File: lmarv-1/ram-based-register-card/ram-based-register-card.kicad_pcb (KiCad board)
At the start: 4 copper layers, 125.4 x 41.3 mm, 18 parts, among them P1 dual-pcie-cardedge, U1 IDT70V24_TQ100, U2 IDT70V24_TQ100, U3 IDT70V24_TQ100, U4 IDT70V24_TQ100

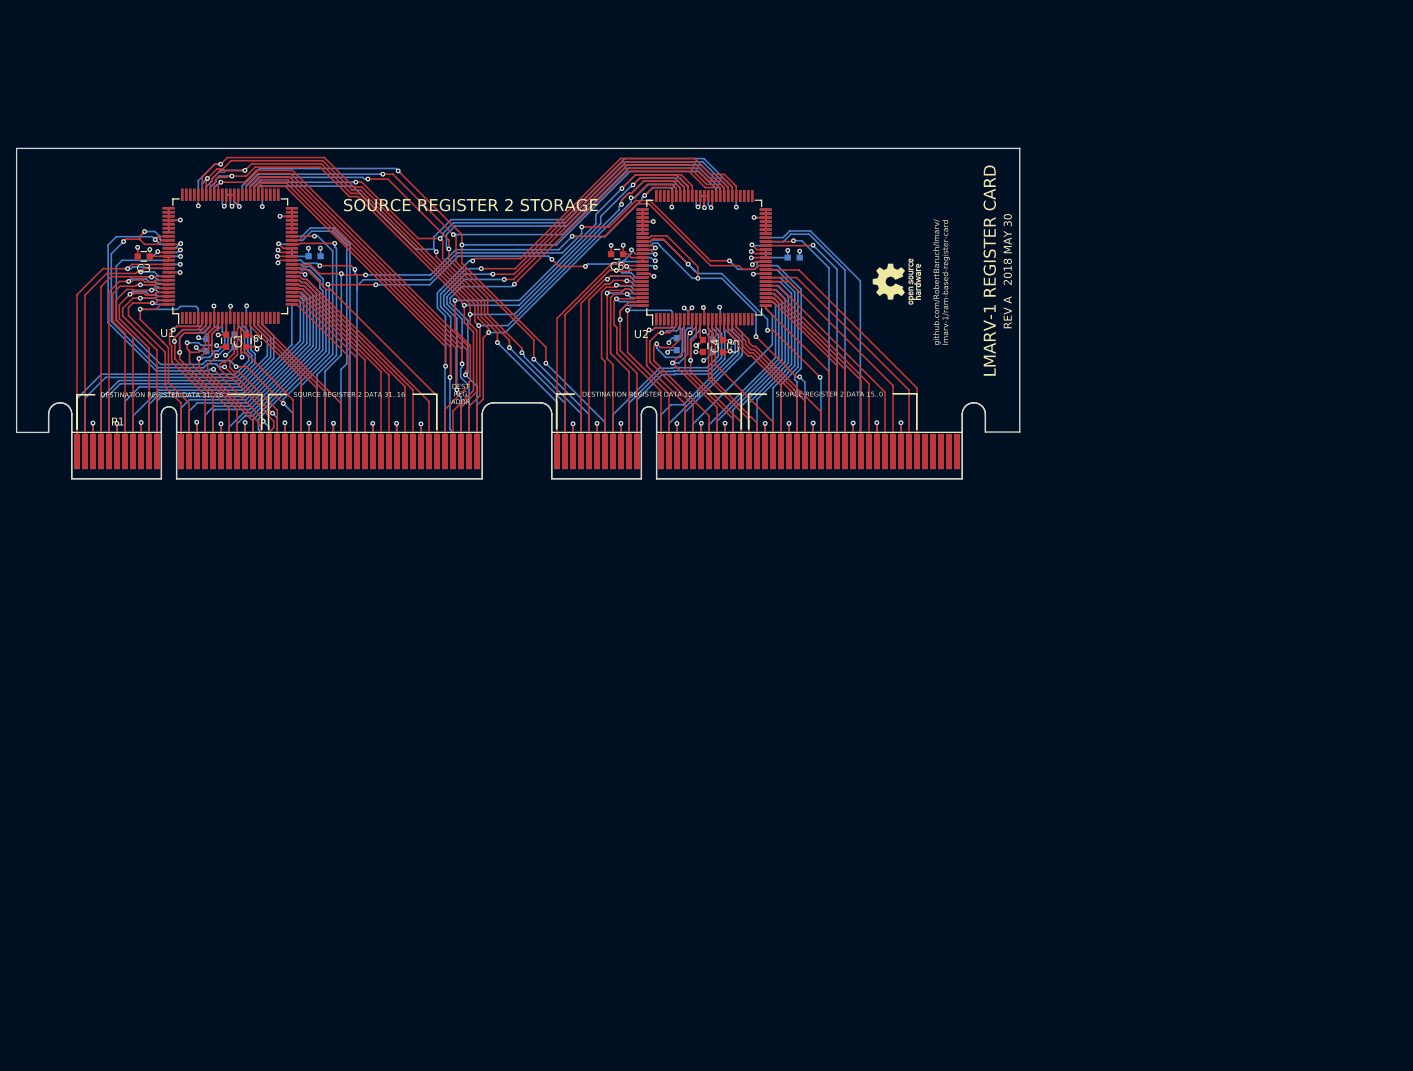
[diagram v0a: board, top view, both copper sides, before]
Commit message: ALU rev D, with simulations
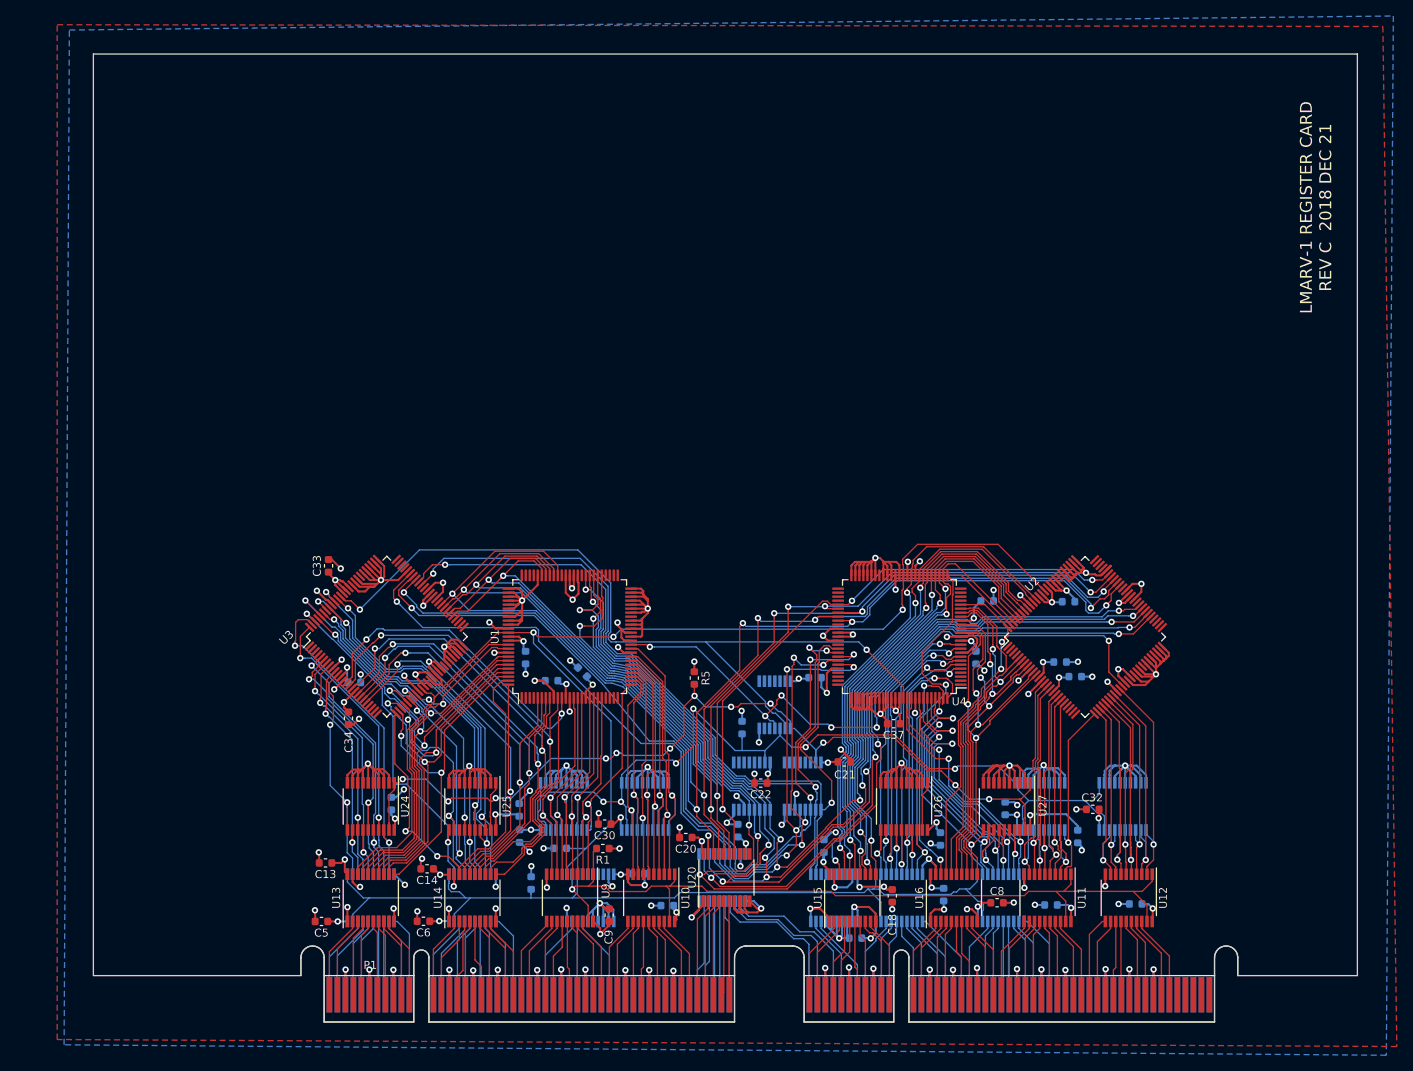
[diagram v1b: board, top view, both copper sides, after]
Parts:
- removed REF***: OSHW-Logo_5.7x6mm_SilkScreen, Symbols:OSHW-Logo_5.7x6mm_SilkScreen
- added C13: 0u1, Capacitor_SMD:C_0603_1608Metric, F.Cu at (93.0, 131.1)
- added C14: 0u1, Capacitor_SMD:C_0603_1608Metric, F.Cu at (105.7, 131.9)
- added C15: 0u1, Capacitor_SMD:C_0603_1608Metric, B.Cu at (155.3, 129.0)
- added C16: 0u1, Capacitor_SMD:C_0603_1608Metric, B.Cu at (170.3, 135.1)
- added C17: 0u1, Capacitor_SMD:C_0603_1608Metric, B.Cu at (132.1, 132.5)
- added C18: 0u1, Capacitor_SMD:C_0603_1608Metric, F.Cu at (163.9, 135.2)
- added C19: 0u1, Capacitor_SMD:C_0603_1608Metric, B.Cu at (144.6, 127.1)
- added C20: 0u1, Capacitor_SMD:C_0603_1608Metric, F.Cu at (138.0, 127.9)
- added C21: 0u1, Capacitor_SMD:C_0603_1608Metric, F.Cu at (157.9, 118.5)
- added C22: 0u1, Capacitor_SMD:C_0603_1608Metric, F.Cu at (147.4, 121.1)
- added C23: 0u1, Capacitor_SMD:C_0603_1608Metric, B.Cu at (154.2, 108.0)
- added C24: 0u1, Capacitor_SMD:C_0603_1608Metric, B.Cu at (101.2, 123.7)
- added C25: 0u1, Capacitor_SMD:C_0603_1608Metric, B.Cu at (117.2, 124.5)
- added C26: 0u1, Capacitor_SMD:C_0603_1608Metric, B.Cu at (169.9, 128.1)
- added C27: 0u1, Capacitor_SMD:C_0603_1608Metric, B.Cu at (187.0, 127.8)
- added C28: 0u1, Capacitor_SMD:C_0603_1608Metric, B.Cu at (186.7, 107.8)
- added C29: 0u1, Capacitor_SMD:C_0603_1608Metric, B.Cu at (117.3, 127.8)
- added C30: 0u1, Capacitor_SMD:C_0603_1608Metric, F.Cu at (127.9, 126.3)
- added C31: 0u1, Capacitor_SMD:C_0603_1608Metric, B.Cu at (178.0, 124.3)
- added C32: 0u1, Capacitor_SMD:C_0603_1608Metric, F.Cu at (188.9, 124.4)
- added C33: 0u1, Capacitor_SMD:C_0603_1608Metric, F.Cu at (93.4, 94.0)
- added C34: 0u1, Capacitor_SMD:C_0603_1608Metric, F.Cu at (95.9, 113.0)
- added C35: 0u1, Capacitor_SMD:C_0603_1608Metric, B.Cu at (185.9, 98.5)
- added C36: 0u1, Capacitor_SMD:C_0603_1608Metric, B.Cu at (184.8, 106.0)
- added C37: 0u1, Capacitor_SMD:C_0603_1608Metric, F.Cu at (164.0, 113.7)
- added C38: 0u1, Capacitor_SMD:C_0603_1608Metric, B.Cu at (175.7, 98.4)
- added C39: 0u1, Capacitor_SMD:C_0603_1608Metric, B.Cu at (174.3, 105.4)
- added R1: 47k, Resistor_SMD:R_0603_1608Metric, F.Cu at (127.7, 129.3)
- added R2: 47k, Resistor_SMD:R_0603_1608Metric, B.Cu at (118.7, 133.6)
- added R3: 47k, Resistor_SMD:R_0603_1608Metric, B.Cu at (122.4, 129.3)
- added R4: 47k, Resistor_SMD:R_0603_1608Metric, B.Cu at (145.1, 114.2)
- added R5: 47k, Resistor_SMD:R_0603_1608Metric, F.Cu at (139.1, 108.0)
- added U10: 74LVC541_a, Package_SO:TSSOP-20_4.4x6.5mm_P0.65mm, F.Cu at (133.7, 135.5)
- added U11: 74LVC541_a, Package_SO:TSSOP-20_4.4x6.5mm_P0.65mm, F.Cu at (183.3, 135.5)
- added U12: 74LVC541_a, Package_SO:TSSOP-20_4.4x6.5mm_P0.65mm, F.Cu at (193.4, 135.5)
- added U13: 74LVC541, Package_SO:TSSOP-20_4.4x6.5mm_P0.65mm, F.Cu at (98.7, 135.5)
- added U14: 74LVC541, Package_SO:TSSOP-20_4.4x6.5mm_P0.65mm, F.Cu at (111.4, 135.5)
- added U15: 74LVC541, Package_SO:TSSOP-20_4.4x6.5mm_P0.65mm, F.Cu at (158.9, 135.5)
- added U16: 74LVC541, Package_SO:TSSOP-20_4.4x6.5mm_P0.65mm, F.Cu at (171.6, 135.5)
- added U17: 74LVC541, Package_SO:TSSOP-20_4.4x6.5mm_P0.65mm, B.Cu at (126.1, 135.5)
- added U18: 74LVC541, Package_SO:TSSOP-20_4.4x6.5mm_P0.65mm, B.Cu at (156.6, 135.5)
- added U19: 74LVC541, Package_SO:TSSOP-20_4.4x6.5mm_P0.65mm, B.Cu at (142.6, 132.9)
- added U20: 74LVC541, Package_SO:TSSOP-20_4.4x6.5mm_P0.65mm, F.Cu at (143.1, 132.9)
- added U21: 74LVC138, Package_SO:TSSOP-16_4.4x5mm_P0.65mm, B.Cu at (152.7, 121.5)
- added U22: 74LVC138, Package_SO:TSSOP-16_4.4x5mm_P0.65mm, B.Cu at (146.3, 121.5)
- added U23: 74LVC04, Package_SO:TSSOP-14_4.4x5mm_P0.65mm, B.Cu at (149.2, 111.3)
- added U24: 74LVC541_a, Package_SO:TSSOP-20_4.4x6.5mm_P0.65mm, F.Cu at (98.7, 124.0)
- added U25: 74LVC541_a, Package_SO:TSSOP-20_4.4x6.5mm_P0.65mm, F.Cu at (111.4, 124.0)
- added U26: 74LVC541_a, Package_SO:TSSOP-20_4.4x6.5mm_P0.65mm, F.Cu at (165.3, 124.0)
- added U27: 74LVC541_a, Package_SO:TSSOP-20_4.4x6.5mm_P0.65mm, F.Cu at (178.2, 124.0)
- added U29: 74LVC541, Package_SO:TSSOP-20_4.4x6.5mm_P0.65mm, B.Cu at (122.8, 124.0)
- added U30: 74LVC541, Package_SO:TSSOP-20_4.4x6.5mm_P0.65mm, B.Cu at (133.0, 124.0)
- added U31: 74LVC541, Package_SO:TSSOP-20_4.4x6.5mm_P0.65mm, B.Cu at (182.5, 124.0)
- added U32: 74LVC541, Package_SO:TSSOP-20_4.4x6.5mm_P0.65mm, B.Cu at (192.7, 124.0)
- added U5: 74LVC541, Package_SO:TSSOP-20_4.4x6.5mm_P0.65mm, B.Cu at (98.7, 135.5)
- added U6: 74LVC541, Package_SO:TSSOP-20_4.4x6.5mm_P0.65mm, B.Cu at (111.4, 135.5)
- added U7: 74LVC541, Package_SO:TSSOP-20_4.4x6.5mm_P0.65mm, B.Cu at (164.7, 135.5)
- added U8: 74LVC541, Package_SO:TSSOP-20_4.4x6.5mm_P0.65mm, B.Cu at (177.4, 135.5)
- added U9: 74LVC541_a, Package_SO:TSSOP-20_4.4x6.5mm_P0.65mm, F.Cu at (123.6, 135.5)
- C1, C2, C3, C4: footprint Capacitors_SMD:C_0603 -> Capacitor_SMD:C_0603_1608Metric; moved to B.Cu
- C10, C11, C12, C5, C6, C7: footprint Capacitors_SMD:C_0603 -> Capacitor_SMD:C_0603_1608Metric
- C8, C9: footprint Capacitors_SMD:C_0603 -> Capacitor_SMD:C_0603_1608Metric; moved to F.Cu
- P1: value dual-pcie-cardedge -> dual-pcie-cardedge_split
- U1, U2: footprint Housings_QFP:TQFP-100_14x14mm_Pitch0.5mm -> Package_QFP:TQFP-100_14x14mm_P0.5mm
- U3, U4: footprint Housings_QFP:TQFP-100_14x14mm_Pitch0.5mm -> Package_QFP:TQFP-100_14x14mm_P0.5mm; moved to F.Cu
- moved C8 121.0 mm to (177.0, 136.1), turned to 0 degrees
- moved C7 107.7 mm to (159.3, 140.5), turned to 180 degrees
- moved C12 91.4 mm to (194.3, 136.2), turned to 180 degrees
- moved C9 90.2 mm to (128.5, 137.6), turned to 90 degrees
- moved C5 87.7 mm to (92.5, 138.4), turned to 180 degrees
- moved C6 86.8 mm to (105.3, 138.4)
- moved C11 81.7 mm to (183.7, 136.4), turned to 180 degrees
- moved C3 75.5 mm to (125.1, 107.3), turned to 135 degrees
- moved P1 74.9 mm to (105.0, 151.0)
- moved C10 70.2 mm to (135.7, 136.4), turned to 180 degrees
- moved U2 67.2 mm to (188.0, 102.9), turned to 45 degrees
- moved U1 63.7 mm to (123.5, 102.8)
- moved C4 60.6 mm to (96.6, 108.6), turned to 0 degrees
- moved C2 57.1 mm to (121.3, 108.3), turned to 180 degrees
- moved C1 54.5 mm to (118.0, 105.4)
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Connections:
- P1 pad 121: /~rd_bhh -> Net-(P1-Pad121)
- P1 pad 122: /~rd_bhl -> Net-(P1-Pad122)
- P1 pad 125: /~rs2_bhh -> Net-(P1-Pad125)
- P1 pad 127: /~rs2_bhl -> Net-(P1-Pad127)
- P1 pad 130: /~rs1_bhh -> Net-(P1-Pad130)
- P1 pad 131: /~rs1_bhl -> Net-(P1-Pad131)
- P1 pad 177: /~rd_blh -> Net-(P1-Pad177)
- P1 pad 179: /~rd_bll -> Net-(P1-Pad179)
- P1 pad 180: /~rs2_blh -> Net-(P1-Pad180)
- P1 pad 181: /~rs2_bll -> Net-(P1-Pad181)
- P1 pad 182: /~rs1_blh -> Net-(P1-Pad182)
- P1 pad 184: /~rs1_bll -> Net-(P1-Pad184)
- U1 pad 10: /rd[17] -> /rd[17]'
- U1 pad 100: /rd[22] -> /rd[22]'
- U1 pad 11: /rd[16] -> /rd[16]'
- U1 pad 14: /rs2[31] -> /rs2[31]'
- U1 pad 15: /rs2[30] -> /rs2[30]'
- U1 pad 16: /rs2[29] -> /rs2[29]'
- U1 pad 18: /rs2[28] -> /rs2[28]'
- U1 pad 19: /rs2[27] -> /rs2[27]'
- U1 pad 20: /rs2[26] -> /rs2[26]'
- U1 pad 21: /rs2[25] -> /rs2[25]'
- U1 pad 26: /rs2[24] -> /rs2[24]'
- U1 pad 27: /rs2[23] -> /rs2[23]'
- U1 pad 28: /rs2[22] -> /rs2[22]'
- U1 pad 29: /rs2[21] -> /rs2[21]'
- U1 pad 30: /rs2[20] -> /rs2[20]'
- U1 pad 31: /rs2[19] -> /rs2[19]'
- U1 pad 32: /rs2[18] -> /rs2[18]'
- U1 pad 33: /rs2[17] -> /rs2[17]'
- U1 pad 35: /rs2[16] -> /rs2[16]'
- U1 pad 36: /~rs2_rd -> /rs2_zero
- U1 pad 41: /~rs2_bhl -> GND
- U1 pad 42: /~rs2_bhh -> GND
- U1 pad 5: /rd[21] -> /rd[21]'
- U1 pad 55: /rs2a[4] -> /rs2a[4]'
- U1 pad 56: /rs2a[3] -> /rs2a[3]'
- U1 pad 57: /rs2a[2] -> /rs2a[2]'
- U1 pad 58: /rs2a[1] -> /rs2a[1]'
- U1 pad 59: /rs2a[0] -> /rs2a[0]'
- U1 pad 6: /rd[20] -> /rd[20]'
- U1 pad 66: /rda[0] -> /rda[0]'
- U1 pad 67: /rda[1] -> /rda[1]'
- U1 pad 68: /rda[2] -> /rda[2]'
- U1 pad 69: /rda[3] -> /rda[3]'
- U1 pad 7: /rd[19] -> /rd[19]'
- U1 pad 70: /rda[4] -> /rda[4]'
- U1 pad 8: /rd[18] -> /rd[18]'
- U1 pad 83: /~rd_bhh -> GND
- U1 pad 84: /~rd_bhl -> GND
- U1 pad 87: /~rd_wr -> /~rd_wr~'
- U1 pad 90: /rd[31] -> /rd[31]'
- U1 pad 91: /rd[30] -> /rd[30]'
- U1 pad 93: /rd[29] -> /rd[29]'
- U1 pad 94: /rd[28] -> /rd[28]'
- U1 pad 95: /rd[27] -> /rd[27]'
- U1 pad 96: /rd[26] -> /rd[26]'
- U1 pad 97: /rd[25] -> /rd[25]'
- U1 pad 98: /rd[24] -> /rd[24]'
- U1 pad 99: /rd[23] -> /rd[23]'
- U2 pad 10: /rd[1] -> /rd[1]'
- U2 pad 100: /rd[6] -> /rd[6]'
- U2 pad 11: /rd[0] -> /rd[0]'
- U2 pad 14: /rs2[15] -> /rs2[15]'
- U2 pad 15: /rs2[14] -> /rs2[14]'
- U2 pad 16: /rs2[13] -> /rs2[13]'
- U2 pad 18: /rs2[12] -> /rs2[12]'
- U2 pad 19: /rs2[11] -> /rs2[11]'
- U2 pad 20: /rs2[10] -> /rs2[10]'
- U2 pad 21: /rs2[9] -> /rs2[9]'
- U2 pad 26: /rs2[8] -> /rs2[8]'
- U2 pad 27: /rs2[7] -> /rs2[7]'
- U2 pad 28: /rs2[6] -> /rs2[6]'
- U2 pad 29: /rs2[5] -> /rs2[5]'
- U2 pad 30: /rs2[4] -> /rs2[4]'
- U2 pad 31: /rs2[3] -> /rs2[3]'
- U2 pad 32: /rs2[2] -> /rs2[2]'
- U2 pad 33: /rs2[1] -> /rs2[1]'
- U2 pad 35: /rs2[0] -> /rs2[0]'
- U2 pad 36: /~rs2_rd -> /rs2_zero
- U2 pad 41: /~rs2_bll -> GND
- U2 pad 42: /~rs2_blh -> GND
- U2 pad 5: /rd[5] -> /rd[5]'
- U2 pad 55: /rs2a[4] -> /rs2a[4]'
- U2 pad 56: /rs2a[3] -> /rs2a[3]'
- U2 pad 57: /rs2a[2] -> /rs2a[2]'
- U2 pad 58: /rs2a[1] -> /rs2a[1]'
- U2 pad 59: /rs2a[0] -> /rs2a[0]'
- U2 pad 6: /rd[4] -> /rd[4]'
- U2 pad 66: /rda[0] -> /rda[0]'
- U2 pad 67: /rda[1] -> /rda[1]'
- U2 pad 68: /rda[2] -> /rda[2]'
- U2 pad 69: /rda[3] -> /rda[3]'
- U2 pad 7: /rd[3] -> /rd[3]'
- U2 pad 70: /rda[4] -> /rda[4]'
- U2 pad 8: /rd[2] -> /rd[2]'
- U2 pad 83: /~rd_blh -> GND
- U2 pad 84: /~rd_bll -> GND
- U2 pad 87: /~rd_wr -> /~rd_wr~'
- U2 pad 90: /rd[15] -> /rd[15]'
- U2 pad 91: /rd[14] -> /rd[14]'
- U2 pad 93: /rd[13] -> /rd[13]'
- U2 pad 94: /rd[12] -> /rd[12]'
- U2 pad 95: /rd[11] -> /rd[11]'
- U2 pad 96: /rd[10] -> /rd[10]'
- U2 pad 97: /rd[9] -> /rd[9]'
- U2 pad 98: /rd[8] -> /rd[8]'
- U2 pad 99: /rd[7] -> /rd[7]'
- U3 pad 10: /rs1[30] -> /rs1[30]'
- U3 pad 100: /rs1[25] -> /rs1[25]'
- U3 pad 11: /rs1[31] -> /rs1[31]'
- U3 pad 14: /rd[16] -> /rd[16]'
- U3 pad 15: /rd[17] -> /rd[17]'
- U3 pad 16: /rd[18] -> /rd[18]'
- U3 pad 18: /rd[19] -> /rd[19]'
- U3 pad 19: /rd[20] -> /rd[20]'
- U3 pad 20: /rd[21] -> /rd[21]'
- U3 pad 21: /rd[22] -> /rd[22]'
- U3 pad 26: /rd[23] -> /rd[23]'
- U3 pad 27: /rd[24] -> /rd[24]'
- U3 pad 28: /rd[25] -> /rd[25]'
- U3 pad 29: /rd[26] -> /rd[26]'
- U3 pad 30: /rd[27] -> /rd[27]'
- U3 pad 31: /rd[28] -> /rd[28]'
- U3 pad 32: /rd[29] -> /rd[29]'
- U3 pad 33: /rd[30] -> /rd[30]'
- U3 pad 35: /rd[31] -> /rd[31]'
- U3 pad 37: /~rd_wr -> /~rd_wr~'
- U3 pad 41: /~rd_bhh -> GND
- U3 pad 42: /~rd_bhl -> GND
- U3 pad 5: /rs1[26] -> /rs1[26]'
- U3 pad 55: /rda[4] -> /rda[4]'
- U3 pad 56: /rda[3] -> /rda[3]'
- U3 pad 57: /rda[2] -> /rda[2]'
- U3 pad 58: /rda[1] -> /rda[1]'
- U3 pad 59: /rda[0] -> /rda[0]'
- U3 pad 6: /rs1[27] -> /rs1[27]'
- U3 pad 66: /rs1a[0] -> /rs1a[0]'
- U3 pad 67: /rs1a[1] -> /rs1a[1]'
- U3 pad 68: /rs1a[2] -> /rs1a[2]'
- U3 pad 69: /rs1a[3] -> /rs1a[3]'
- U3 pad 7: /rs1[28] -> /rs1[28]'
- U3 pad 70: /rs1a[4] -> /rs1a[4]'
- U3 pad 8: /rs1[29] -> /rs1[29]'
- U3 pad 83: /~rs1_bhl -> GND
- U3 pad 84: /~rs1_bhh -> GND
- U3 pad 89: /~rs1_rd -> /rs1_zero
- U3 pad 90: /rs1[16] -> /rs1[16]'
- U3 pad 91: /rs1[17] -> /rs1[17]'
- U3 pad 93: /rs1[18] -> /rs1[18]'
- U3 pad 94: /rs1[19] -> /rs1[19]'
- U3 pad 95: /rs1[20] -> /rs1[20]'
- U3 pad 96: /rs1[21] -> /rs1[21]'
- U3 pad 97: /rs1[22] -> /rs1[22]'
- U3 pad 98: /rs1[23] -> /rs1[23]'
- U3 pad 99: /rs1[24] -> /rs1[24]'
- U4 pad 10: /rs1[14] -> /rs1[14]'
- U4 pad 100: /rs1[9] -> /rs1[9]'
- U4 pad 11: /rs1[15] -> /rs1[15]'
- U4 pad 14: /rd[0] -> /rd[0]'
- U4 pad 15: /rd[1] -> /rd[1]'
- U4 pad 16: /rd[2] -> /rd[2]'
- U4 pad 18: /rd[3] -> /rd[3]'
- U4 pad 19: /rd[4] -> /rd[4]'
- U4 pad 20: /rd[5] -> /rd[5]'
- U4 pad 21: /rd[6] -> /rd[6]'
- U4 pad 26: /rd[7] -> /rd[7]'
- U4 pad 27: /rd[8] -> /rd[8]'
- U4 pad 28: /rd[9] -> /rd[9]'
- U4 pad 29: /rd[10] -> /rd[10]'
- U4 pad 30: /rd[11] -> /rd[11]'
- U4 pad 31: /rd[12] -> /rd[12]'
- U4 pad 32: /rd[13] -> /rd[13]'
- U4 pad 33: /rd[14] -> /rd[14]'
- U4 pad 35: /rd[15] -> /rd[15]'
- U4 pad 37: /~rd_wr -> /~rd_wr~'
- U4 pad 41: /~rd_blh -> GND
- U4 pad 42: /~rd_bll -> GND
- U4 pad 5: /rs1[10] -> /rs1[10]'
- U4 pad 55: /rda[4] -> /rda[4]'
- U4 pad 56: /rda[3] -> /rda[3]'
- U4 pad 57: /rda[2] -> /rda[2]'
- U4 pad 58: /rda[1] -> /rda[1]'
- U4 pad 59: /rda[0] -> /rda[0]'
- U4 pad 6: /rs1[11] -> /rs1[11]'
- U4 pad 66: /rs1a[0] -> /rs1a[0]'
- U4 pad 67: /rs1a[1] -> /rs1a[1]'
- U4 pad 68: /rs1a[2] -> /rs1a[2]'
- U4 pad 69: /rs1a[3] -> /rs1a[3]'
- U4 pad 7: /rs1[12] -> /rs1[12]'
- U4 pad 70: /rs1a[4] -> /rs1a[4]'
- U4 pad 8: /rs1[13] -> /rs1[13]'
- U4 pad 83: /~rs1_bll -> GND
- U4 pad 84: /~rs1_blh -> GND
- U4 pad 89: /~rs1_rd -> /rs1_zero
- U4 pad 90: /rs1[0] -> /rs1[0]'
- U4 pad 91: /rs1[1] -> /rs1[1]'
- U4 pad 93: /rs1[2] -> /rs1[2]'
- U4 pad 94: /rs1[3] -> /rs1[3]'
- U4 pad 95: /rs1[4] -> /rs1[4]'
- U4 pad 96: /rs1[5] -> /rs1[5]'
- U4 pad 97: /rs1[6] -> /rs1[6]'
- U4 pad 98: /rs1[7] -> /rs1[7]'
- U4 pad 99: /rs1[8] -> /rs1[8]'
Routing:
- net GND: track 222.0 -> 706.3 mm, vias 56 -> 113
- net /rda[0]': track 0.00 -> 153.0 mm, vias 0 -> 5
- net /rda[1]': track 0.00 -> 148.5 mm, vias 0 -> 5
- net /rda[2]': track 0.00 -> 145.4 mm, vias 0 -> 5
- net /rs2a[4]': track 0.00 -> 139.5 mm, vias 0 -> 5
- net /rda[3]': track 0.00 -> 138.9 mm, vias 0 -> 5
- net /rs2a[2]': track 0.00 -> 136.2 mm, vias 0 -> 5
- net /rs2a[3]': track 0.00 -> 134.9 mm, vias 0 -> 5
- net /rda[4]': track 0.00 -> 133.5 mm, vias 0 -> 4
- net /~rd_wr~': track 0.00 -> 130.4 mm, vias 0 -> 3
- net /rs2a[1]': track 0.00 -> 128.8 mm, vias 0 -> 5
- net /rs2a[0]': track 0.00 -> 126.8 mm, vias 0 -> 5
- net /~rs1_zero: track 0.00 -> 126.6 mm, vias 0 -> 12
- net /~rs2_zero: track 0.00 -> 114.6 mm, vias 0 -> 6
- net VCC: track 134.1 -> 247.6 mm, vias 33 -> 65
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- added copper zone on B.Cu, net GND
- added copper zone on F.Cu, net GND
- added copper zone on In1.Cu, net GND
- added copper zone on In2.Cu, net VCC
- removed copper zone on GND, net GND
- removed copper zone on VCC, net VCC
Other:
- board size 125.4 x 41.3 mm -> 158 x 115.2 mm
- net class Default: clearance 0.2 -> 0.1524; trace_width 0.2 -> 0.1524; via_dia 0.6 -> 0.8; via_drill 0.3 -> 0.4
- net class Power added: clearance 0.178, trace_width 0.254, via_dia 0.8, via_drill 0.4
- rule trace_clearance: 0.2 -> 0.1524
- rule trace_min: 0.2 -> 0.1524
- board text added: "LMARV-1 REGISTER CARD REV C 2018 DEC 21"
- board text removed: "/RD_BHH"
- board text removed: "/RD_BHL"
- board text removed: "/RD_BLH"
- board text removed: "/RD_BLL"
- board text removed: "/RD_WR"
- board text removed: "/RS1_BHH"
- board text removed: "/RS1_BHL"
- board text removed: "/RS1_BLH"
- board text removed: "/RS1_BLL"
- board text removed: "/RS1_RD"
- board text removed: "/RS2_BHH"
- board text removed: "/RS2_BHL"
- board text removed: "/RS2_BLH"
- board text removed: "/RS2_BLL"
- board text removed: "/RS2_RD"
- board text removed: "DEST REG ADDR"
- board text removed: "DESTINATION REGISTER DATA 15..0"
- board text removed: "DESTINATION REGISTER DATA 31..16"
- board text removed: "LMARV-1 REGISTER CARD"
- board text removed: "REV A 2018 MAY 30"
- board text removed: "SOURCE REG 1 ADDR"
- board text removed: "SOURCE REG 2 ADDR"
- board text removed: "SOURCE REGISTER 1 DATA 0..15"
- board text removed: "SOURCE REGISTER 1 DATA 16..31"
- board text removed: "SOURCE REGISTER 1 STORAGE"
- board text removed: "SOURCE REGISTER 2 DATA 15..0"
- board text removed: "SOURCE REGISTER 2 DATA 31..16"
- board text removed: "SOURCE REGISTER 2 STORAGE"
- board text removed: "github.com/RobertBaruch/lmarv/ lmarv-1/ram-based-register-card"
